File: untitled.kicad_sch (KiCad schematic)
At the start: 23 parts, among them U5 RP2040, U6 W25Q128JVS, U7 E22-900M30S, Y1 ABM8-272-T3

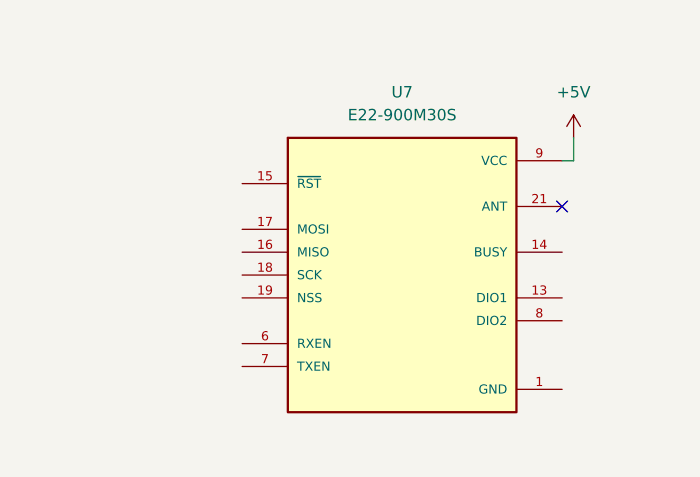
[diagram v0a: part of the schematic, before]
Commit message: add the rest of the components and the OCD connections
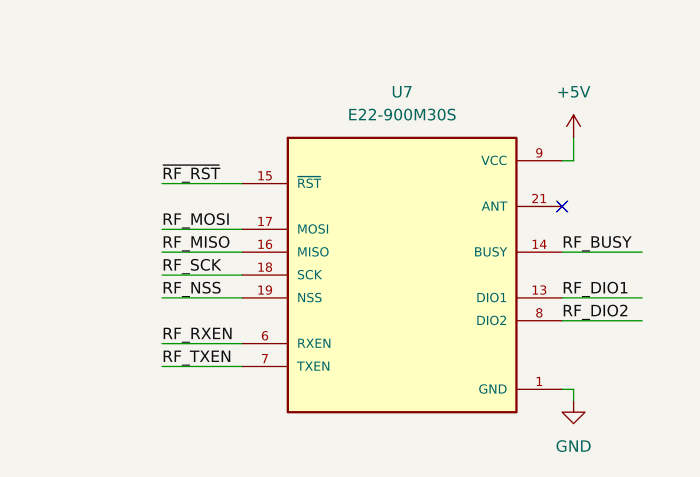
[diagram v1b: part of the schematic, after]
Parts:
- R3, R4, R5, R6, R7: footprint Resistor_SMD:R_0201_0603Metric -> Resistor_SMD:R_0603_1608Metric
- U7: footprint E22:XCVR_E22-900M30S -> E22P:XCVR_E22-900M30S
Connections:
- net RF_DIO1: now reaches U7.13 (DIO1)
- net RF_BUSY: now reaches U7.14 (BUSY)
- net ~{RF_RST}: now reaches U7.15 (~{RST})
- net RF_MISO: now reaches U7.16 (MISO)
- net RF_MOSI: now reaches U7.17 (MOSI)
- net RF_SCK: now reaches U7.18 (SCK)
- net RF_NSS: now reaches U7.19 (NSS)
- net RF_RXEN: now reaches U7.6 (RXEN)
- net RF_TXEN: now reaches U7.7 (TXEN)
- net RF_DIO2: now reaches U7.8 (DIO2)

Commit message: place all components
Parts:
- added P1: USB_C_Plug_USB2.0, Connector_USB:USB_C_Receptacle_GCT_USB4110, symbol Connector:USB_C_Plug_USB2.0
- added R8: 10k, Resistor_SMD:R_0402_1005Metric, symbol Device:R_Small
- added R9: 5K1, Resistor_SMD:R_0603_1608Metric, symbol Device:R_US
- added SW1, SW2: SW_SPST, Button_Switch_SMD:SW_Push_1P1T_NO_CK_KMR2, symbol Switch:SW_SPST
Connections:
- net GND: now also P1.A1 (GND), P1.A12 (GND), P1.B1 (GND), P1.B12 (GND), P1.S1 (SHIELD), R9.2, SW1.1 (A), SW2.1 (A); no longer R4.1, U5.20 (XIN)
- net R_RUN: now also R8.2, SW2.2 (B)
- net R_USB_DM: now also P1.A7 (D-)
- net R_USB_DP: now also P1.A6 (D+)
- net R_X_OUT: now also R4.1; no longer R4.2
- net at C2.2, Y1.3: now also R4.2
- net R_X_IN: now reaches C3.1, Y1.1
- net R_X_IN: now also U5.20 (XIN)
- new net: P1.A4 (VBUS), P1.A9 (VBUS), P1.B4 (VBUS), P1.B9 (VBUS)
- new net: P1.A5 (CC), R9.1
- new net +3V3: R8.1
- new net R_USB_ BOOT: SW1.2 (B)
- no-connect marks 1 -> 3
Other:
- note added: "1U Needs to be placed near V_REG and V_OUT"
- note added: "Boot Mode / Reset SW"
- note added: "Bypass Caps"
- note added: "C = 2 * (C_L - C_Stray) C_Stray = few pF"
- note added: "Requires the connector for the host to been orientated correctly. On one of the CC pins are being shorted to ground via the 5.1K Resisto"
- note added: "USB Interface"
- moved on the sheet: C10, C11, C12, C13, C14, C2, C3, C4, C5, C6, C7, C8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

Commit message: more of the layout
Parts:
- removed P1: USB_C_Plug_USB2.0, Connector_USB:USB_C_Receptacle_GCT_USB4110, symbol Connector:USB_C_Plug_USB2.0
- removed R9: 5K1, Resistor_SMD:R_0603_1608Metric, symbol Device:R_US
- added J2: USB_B_Mini, Connector_USB:USB_Mini-B_Lumberg_2486_01_Horizontal, symbol Connector:USB_B_Mini
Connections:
- net GND: now also J2.5 (GND), J2.6 (Shield)
- net RF_BUSY: now also U5.5 (GPIO3)
- net RF_DIO1: now also U5.4 (GPIO2)
- net RF_DIO2: now also U5.12 (GPIO9)
- net RF_MISO: now also U5.7 (GPIO5)
- net RF_MOSI: now also U5.8 (GPIO6)
- net RF_NSS: now also U5.11 (GPIO8)
- net RF_RXEN: now also U5.14 (GPIO11)
- net RF_SCK: now also U5.9 (GPIO7)
- net RF_TXEN: now also U5.13 (GPIO10)
- net R_USB_DM: now also J2.3 (D+)
- net R_USB_DP: now also J2.2 (D-)
- net ~{RF_RST}: now also U5.6 (GPIO4)
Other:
- note removed: "Requires the connector for the host to been orientated correctly. On one of the CC pins are being shorted to ground via the 5.1K Resisto"

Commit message: route more of the layout
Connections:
- net R_USB_ BOOT is gone; now on net R_USB_BOOT: SW1.2 (B)
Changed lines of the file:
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@@
 		)
 	)
-	(label "R_USB_ BOOT"
+	(label "R_USB_BOOT"
 		(at 39.37 184.15 0)
 		(effects
@@
 			)
 			(justify right bottom)
+		)
+	)
+	(label "R_USB_BOOT"
+		(at 30.48 60.96 0)
+		(effects
+			(font
+				(size 1.27 1.27)
+			)
+			(justify left bottom)
 		)
 	)
@@
 		(effects
 			(font
-				(size 1.27 1.27)
-			)
-			(justify left bottom)
-		)
-	)
-	(label "R_USB_BOOT"
-		(at 30.48 60.96 0)
-		(effects
-			(font

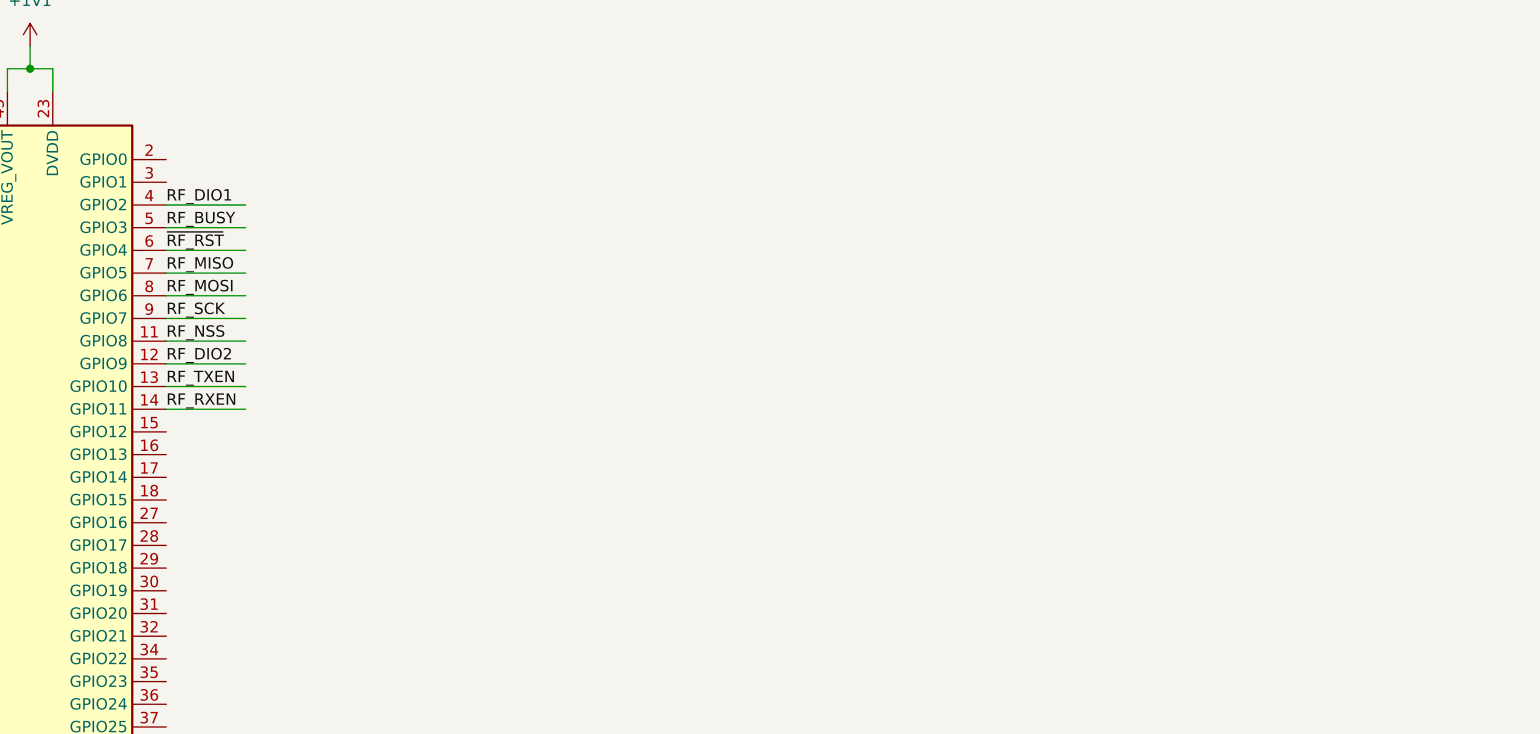
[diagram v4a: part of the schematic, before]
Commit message: update schematic to files and add integration test
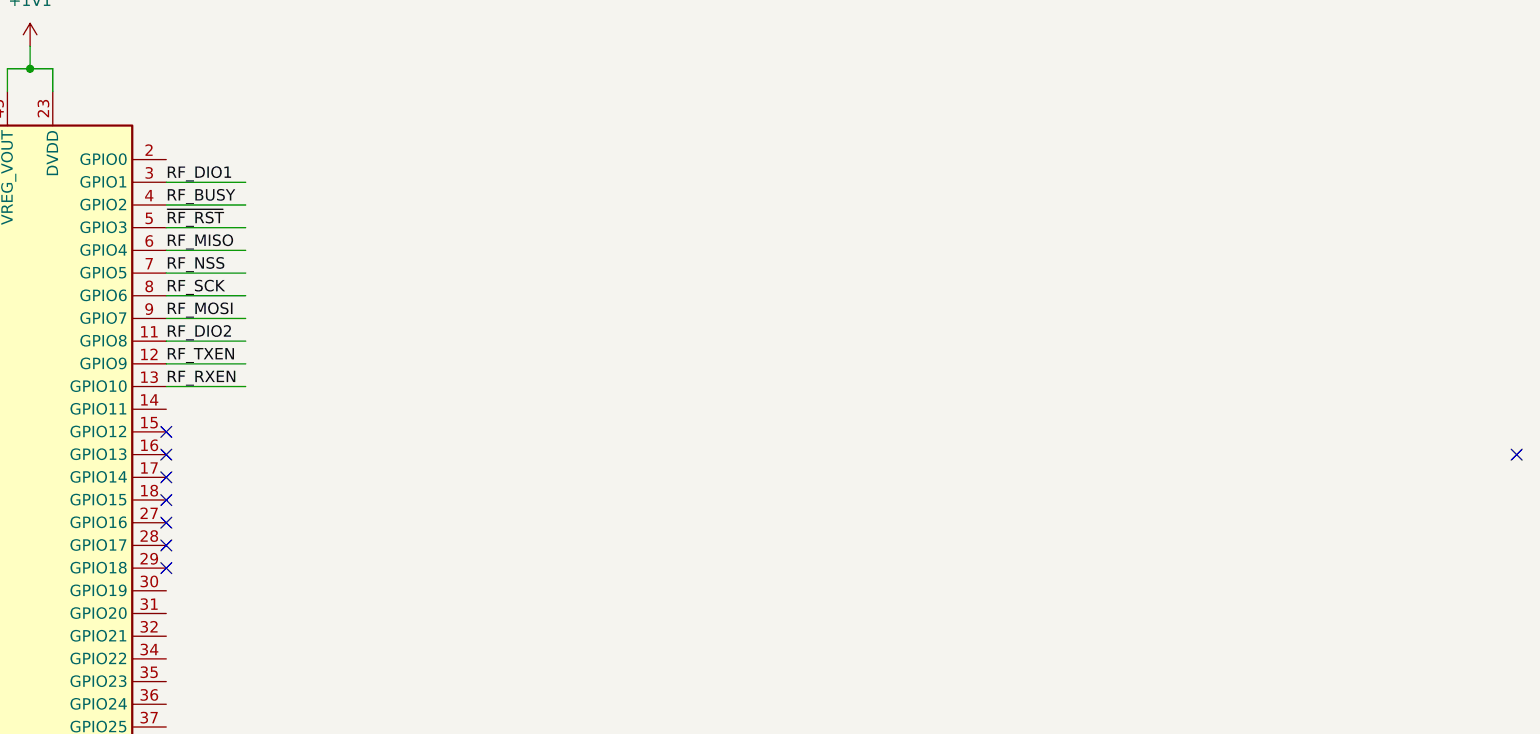
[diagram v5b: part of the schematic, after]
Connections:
- net RF_BUSY: now also U5.4 (GPIO2); no longer U5.5 (GPIO3)
- net RF_DIO1: now also U5.3 (GPIO1); no longer U5.4 (GPIO2)
- net RF_DIO2: now also U5.11 (GPIO8); no longer U5.12 (GPIO9)
- net RF_MISO: now also U5.6 (GPIO4); no longer U5.7 (GPIO5)
- net RF_MOSI: now also U5.9 (GPIO7); no longer U5.8 (GPIO6)
- net RF_NSS: now also U5.7 (GPIO5); no longer U5.11 (GPIO8)
- net RF_RXEN: now also U5.13 (GPIO10); no longer U5.14 (GPIO11)
- net RF_SCK: now also U5.8 (GPIO6); no longer U5.9 (GPIO7)
- net RF_TXEN: now also U5.12 (GPIO9); no longer U5.13 (GPIO10)
- net ~{RF_RST}: now also U5.5 (GPIO3); no longer U5.6 (GPIO4)
- no-connect marks 3 -> 11

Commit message: more cleanup of the schematic
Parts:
- removed R8: 10k, Resistor_SMD:R_0402_1005Metric, symbol Device:R_Small
- added R9: 10K, Resistor_SMD:R_0603_1608Metric, symbol Device:R_US
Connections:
- net +3.3V: now also R9.2
- net R_RUN: now also R9.1
- net R_RX: now reaches U5.15 (GPIO12)
- net R_TX: now reaches U5.16 (GPIO13)
- no-connect marks 11 -> 39

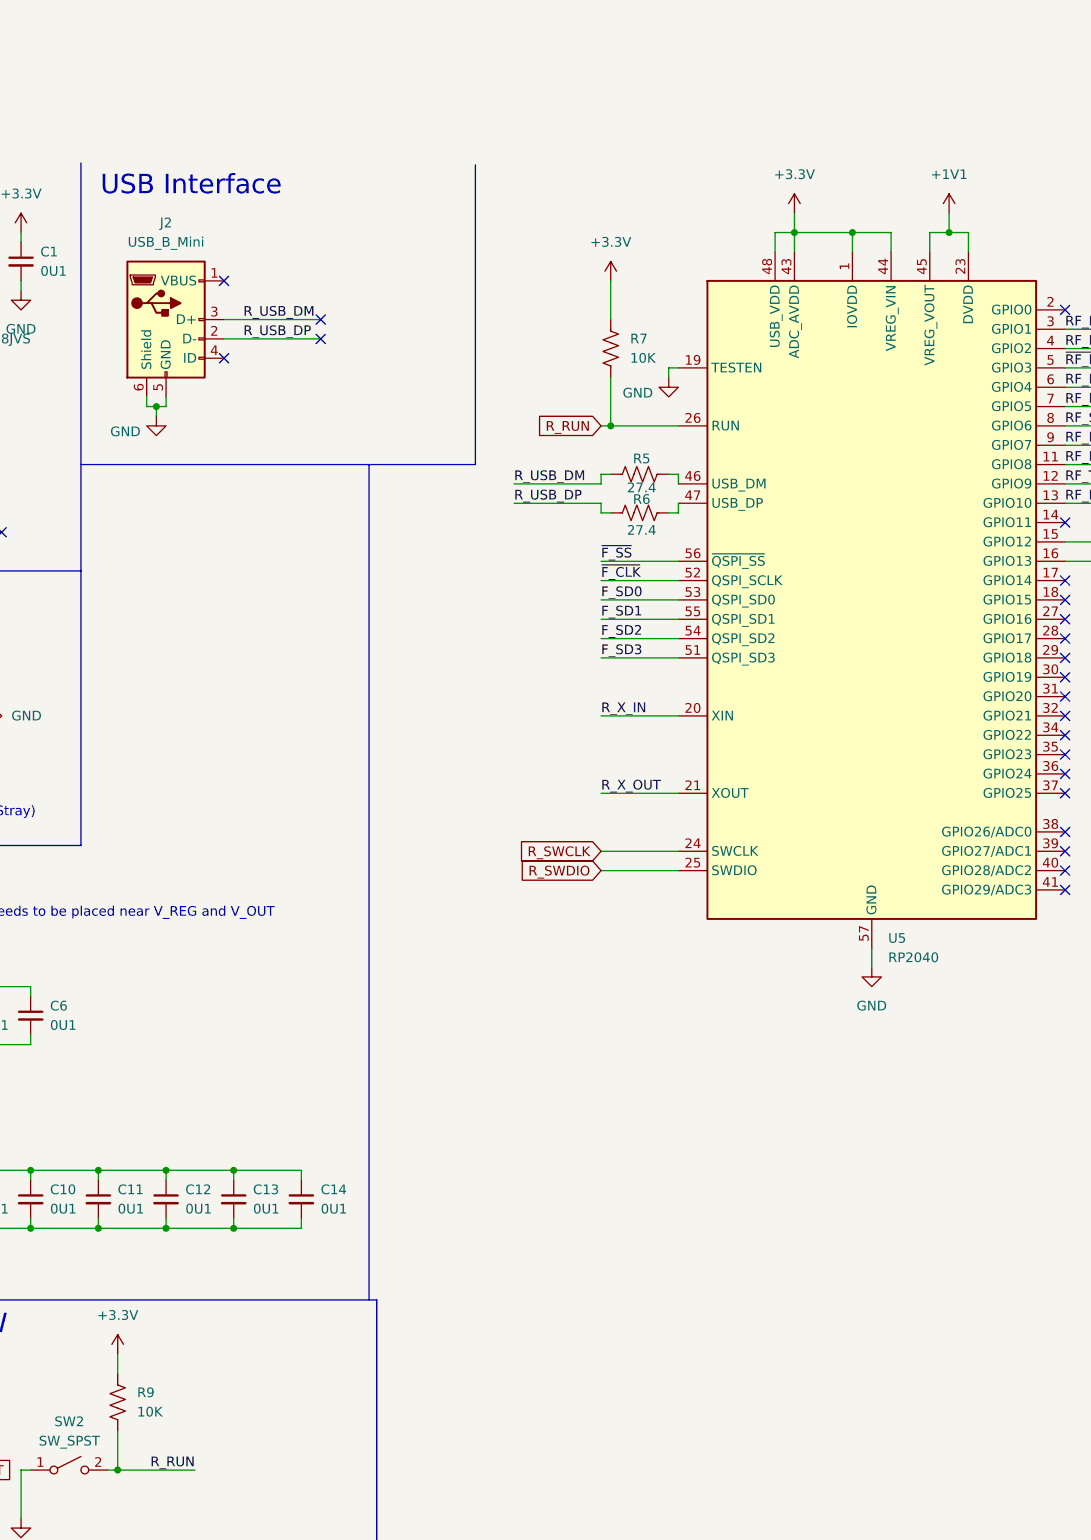
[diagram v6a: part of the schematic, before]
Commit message: add integration test arduino script
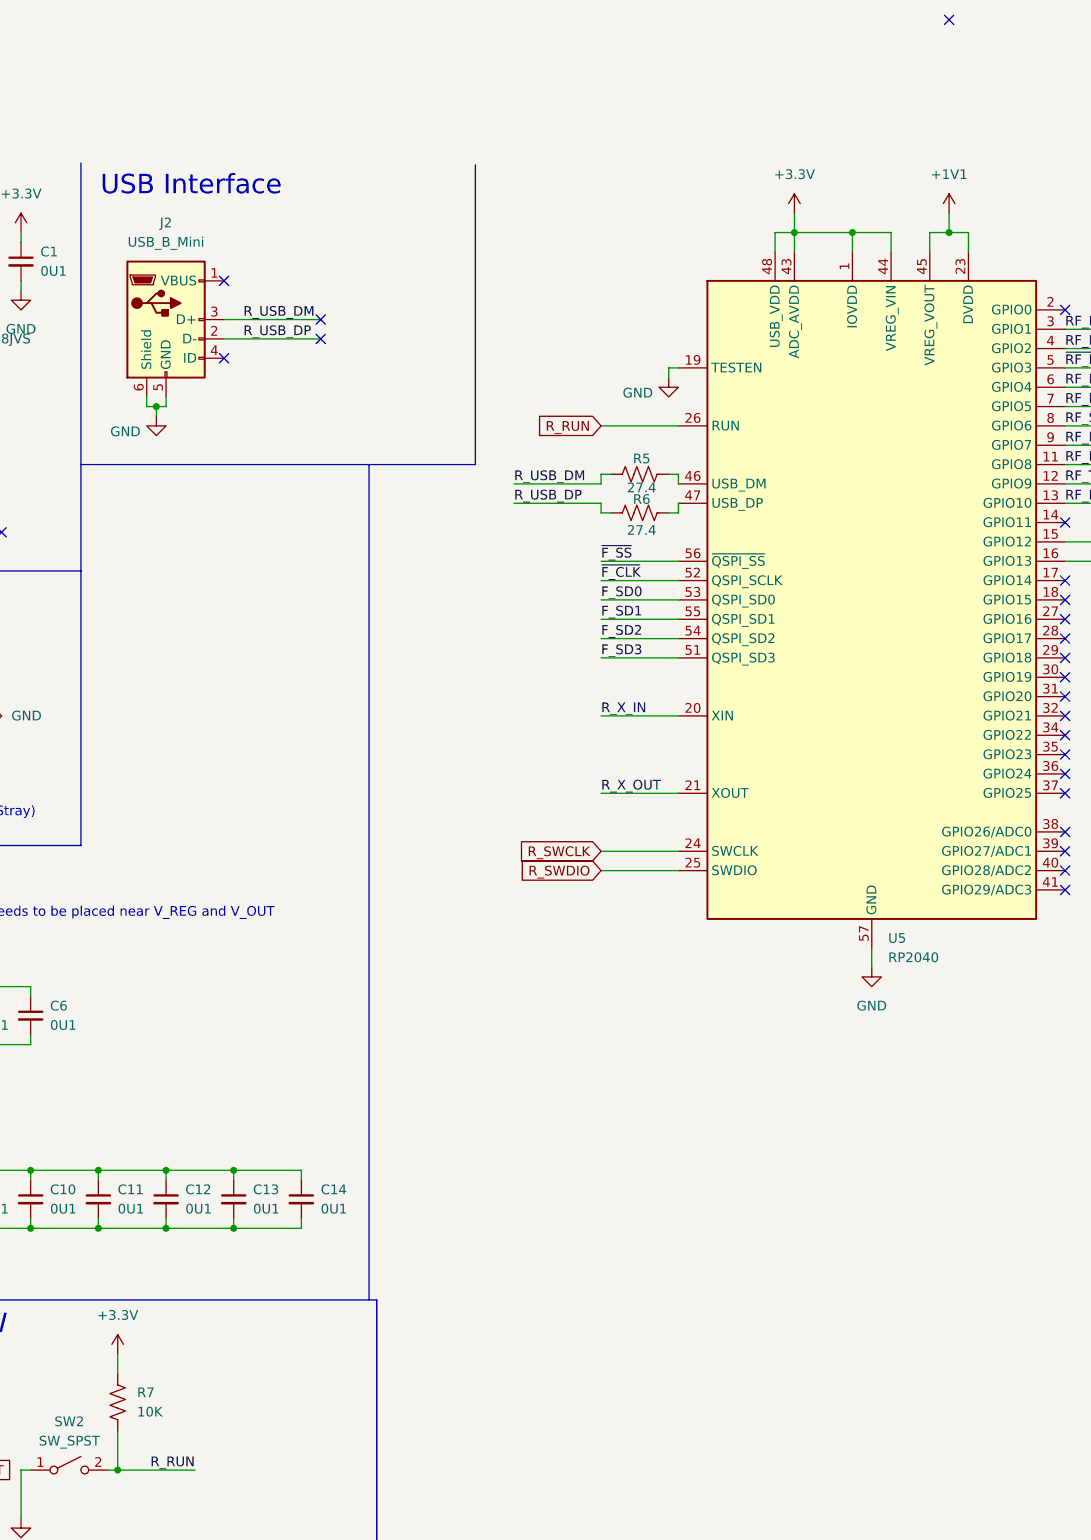
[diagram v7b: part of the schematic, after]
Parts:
- removed R7: 10K, Resistor_SMD:R_0603_1608Metric, symbol Device:R_US
- renumbered R9 to R7
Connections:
- no-connect marks 39 -> 40
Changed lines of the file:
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@@
 	)
 	(junction
-		(at 133.35 46.99)
-		(diameter 0)
-		(color 0 0 0 0)
-	)
-	(junction
 		(at 66.04 152.4)
 		(diameter 0)
@@
 	)
 	(no_connect
+		(at 177.8 -6.35)
+	)
+	(no_connect
 		(at 201.93 44.45)
 	)
@@
 	(wire
 		(pts
-			(xy 133.35 40.64) (xy 133.35 46.99)
-		)
-		(stroke
-			(width 0)
-			(type default)
-		)
-	)
-	(wire
-		(pts
 			(xy 66.04 144.78) (xy 74.93 144.78)
 		)
@@
 	(wire
 		(pts
-			(xy 133.35 46.99) (xy 142.24 46.99)
+			(xy 132.08 46.99) (xy 142.24 46.99)
 		)
 		(stroke
@@
 	(wire
 		(pts
-			(xy 132.08 46.99) (xy 133.35 46.99)
-		)
-		(stroke
-			(width 0)
-			(type default)
-		)
-	)
-	(wire
-		(pts
 			(xy 38.1 184.15) (xy 40.64 184.15)
 		)
@@
 	(wire
 		(pts
-			(xy 133.35 27.94) (xy 133.35 33.02)
-		)
-		(stroke
-			(width 0)
-			(type default)
-		)
-	)
-	(wire
-		(pts
 			(xy 120.65 57.15) (xy 132.08 57.15)
 		)
@@
 		(dnp no)
 		(fields_autoplaced yes)
-		(property "Reference" "R9"
+		(property "Reference" "R7"
 			(at 71.12 173.9899 0)
 			(show_name no)
@@
 			(project "MeshHat"
 				(path "/ac5b0951-7b7b-41d2-b78c-2a2e4b31a9ff/f071743a-4e4f-466f-b4e9-a324f1150a8f"
-					(reference "R9")
+					(reference "R7")
 					(unit 1)
 				)
@@
 	)
 	(symbol
-		(lib_id "Device:R_US")
-		(at 133.35 36.83 0)
-		(unit 1)
-		(body_style 1)
-		(exclude_from_sim no)
-		(in_bom yes)
-		(on_board yes)
-		(in_pos_files yes)
-		(dnp no)
-		(fields_autoplaced yes)
-		(property "Reference" "R7"
-			(at 135.89 35.5599 0)
-			(show_name no)
-			(do_not_autoplace no)
-			(effects
-				(font
-					(size 1.27 1.27)
-				)
-				(justify left)
-			)
-		)
-		(property "Value" "10K"
-			(at 135.89 38.0999 0)
-			(show_name no)
-			(do_not_autoplace no)
-			(effects
-				(font
-					(size 1.27 1.27)
-				)
-				(justify left)
-			)
-		)
-		(property "Footprint" "Resistor_SMD:R_0603_1608Metric"
-			(at 134.366 37.084 90)
-			(hide yes)
-			(show_name no)
-			(do_not_autoplace no)
-			(effects
-				(font
-					(size 1.27 1.27)
-				)
-			)
-		)
-		(property "Datasheet" ""
-			(at 133.35 36.83 0)
-			(hide yes)
-			(show_name no)
-			(do_not_autoplace no)
-			(effects
-				(font
-					(size 1.27 1.27)
-				)
-			)
-		)
-		(property "Description" "Resistor, US symbol"
-			(at 133.35 36.83 0)
-			(hide yes)
-			(show_name no)
-			(do_not_autoplace no)
-			(effects
-				(font
-					(size 1.27 1.27)
-				)
-			)
-		)
-		(pin "1"
-		)
-		(pin "2"
-		)
-		(instances
-			(project "MeshHat"
-				(path "/ac5b0951-7b7b-41d2-b78c-2a2e4b31a9ff/f071743a-4e4f-466f-b4e9-a324f1150a8f"
-					(reference "R7")
-					(unit 1)
-				)
-			)
-		)
-	)
-	(symbol
 		(lib_id "Switch:SW_SPST")
 		(at 62.23 184.15 0)
@@
 					(unit 1)
 				)
-			)
-		)
-	)
-	(symbol
-		(lib_id "power:+3.3V")
-		(at 133.35 27.94 0)
-		(unit 1)
-		(body_style 1)
-		(exclude_from_sim no)
-		(in_bom yes)
-		(on_board yes)
-		(in_pos_files yes)
-		(dnp no)
-		(fields_autoplaced yes)
-		(property "Reference" "#PWR013"
-			(at 133.35 31.75 0)
-			(hide yes)
-			(show_name no)
-			(do_not_autoplace no)
-			(effects
-				(font
-					(size 1.27 1.27)
-				)
-			)
-		)
-		(property "Value" "+3.3V"
-			(at 133.35 22.86 0)
-			(show_name no)
-			(do_not_autoplace no)
-			(effects
-				(font
-					(size 1.27 1.27)
-				)
-			)
-		)
-		(property "Footprint" ""
-			(at 133.35 27.94 0)
-			(hide yes)
-			(show_name no)
-			(do_not_autoplace no)
-			(effects
-				(font
-					(size 1.27 1.27)
-				)
-			)
-		)
-		(property "Datasheet" ""
-			(at 133.35 27.94 0)
-			(hide yes)
-			(show_name no)
-			(do_not_autoplace no)
-			(effects
-				(font
-					(size 1.27 1.27)
-				)
-			)
-		)
-		(property "Description" "Power symbol creates a global label with name \"+3.3V\""
-			(at 133.35 27.94 0)
-			(hide yes)
-			(show_name no)
-			(do_not_autoplace no)
-			(effects
-				(font
-					(size 1.27 1.27)
-				)
-			)
-		)
-		(pin "1"
-		)
-		(instances
-			(project "MeshHat"
-				(path "/ac5b0951-7b7b-41d2-b78c-2a2e4b31a9ff/f071743a-4e4f-466f-b4e9-a324f1150a8f"
-					(reference "#PWR013")
-					(unit 1)
-				)

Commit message: get most of the changes in
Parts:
- added C16, C18: 0U1, Capacitor_SMD:C_0603_1608Metric, symbol Device:C_Small
- added C17: 1U, Capacitor_SMD:C_0603_1608Metric, symbol Device:C_Small
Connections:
- net +3.3V: now also C16.1
- net +5V: now also C17.1, C18.1
- net GND: now also C16.2, C17.2, C18.2
- no-connect marks 40 -> 39
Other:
- note added: "Ebyte E22P LoRa Module"
- moved on the sheet: C10, C11, C12, C13, C14, C7, C8, C9, U7
